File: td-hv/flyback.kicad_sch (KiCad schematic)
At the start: 54 parts, among them Q12 G3R450MT17J, U13 MCP1416

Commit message: td-hv 2.0 changes
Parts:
- removed TP11, TP5: TestPoint, TestPoint:TestPoint_Keystone_5019_Minature, symbol Connector:TestPoint
- added U? (x2): 74HC00, Package_SO:SOIC-14_3.9x8.7mm_P1.27mm, symbol 74xx:74HC00
- C?: footprint Capacitor_SMD:C_1206_3216Metric -> Capacitor_SMD:C_1812_4532Metric
- D?: footprint Diode_SMD:D_SMA -> Diode_THT:D_DO-41_SOD81_P10.16mm_Horizontal
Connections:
- net GND: now also U?.1, U?.1, U?.2, U?.2
- net eht out: now also R?.1; no longer C?.1
- net at C?.2, L?.2, Q?.1 (S)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: now also C?.2; no longer R?.2
- new net snub: C?.1, R?.2
- no-connect marks 4 -> 6
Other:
- moved on the sheet: C?, R?

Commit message: small bom changes
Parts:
- C?: Digikey 1276-3272-1-ND‎ -> 478-3005-1-ND
- D?: value ES1G-13-F -> DNP; footprint Diode_THT:D_DO-41_SOD81_P10.16mm_Horizontal -> Diode_SMD:D_SMA; symbol Diode:BA157 -> Diode:MRA4004T3G
- L?: Digikey (none) -> DNP
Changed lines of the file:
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@@
       (effects (font (size 1.27 1.27)) hide)
     )
-    (property "Digikey" "" (at 161.29 66.04 0)
+    (property "Digikey" "DNP" (at 161.29 66.04 0)
       (effects (font (size 1.27 1.27)) hide)
     )
@@
     )
   )
-  (symbol (lib_id "Diode:BA157") (at 109.22 44.45 180) (unit 1)
+  (symbol (lib_id "Diode:MRA4004T3G") (at 109.22 44.45 180) (unit 1)
     (in_bom yes) (on_board yes) (dnp no)
     (property "Reference" "D?" (at 109.22 38.9636 0)
       (effects (font (size 1.27 1.27)))
     )
-    (property "Value" "ES1G-13-F" (at 109.22 41.275 0)
-      (effects (font (size 1.27 1.27)))
-    )
-    (property "Footprint" "Diode_THT:D_DO-41_SOD81_P10.16mm_Horizontal" (at 109.22 40.005 0)
-      (effects (font (size 1.27 1.27)) hide)
-    )
-    (property "Datasheet" "https://www.vishay.com/docs/88536/ba157.pdf" (at 109.22 44.45 0)
+    (property "Value" "DNP" (at 109.22 41.275 0)
+      (effects (font (size 1.27 1.27)))
+    )
+    (property "Footprint" "Diode_SMD:D_SMA" (at 109.22 40.005 0)
+      (effects (font (size 1.27 1.27)) hide)
+    )
+    (property "Datasheet" "http://www.onsemi.com/pub_link/Collateral/MRA4003T3-D.PDF" (at 109.22 44.45 0)
       (effects (font (size 1.27 1.27)) hide)
     )
@@
       (effects (font (size 1.27 1.27)) hide)
     )
-    (property "Digikey" "1276-3272-1-ND‎" (at 144.78 54.61 0)
-      (effects (font (size 1.27 1.27)) hide)
-    )
+    (property "Digikey" "478-3005-1-ND" (at 144.78 54.61 0)
+      (effects (font (size 1.27 1.27)) hide)
+    )

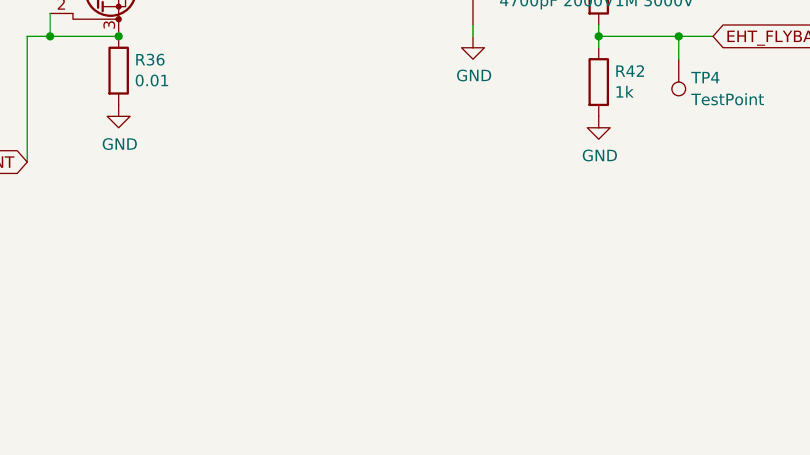
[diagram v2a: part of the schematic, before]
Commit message: add td-hv todo
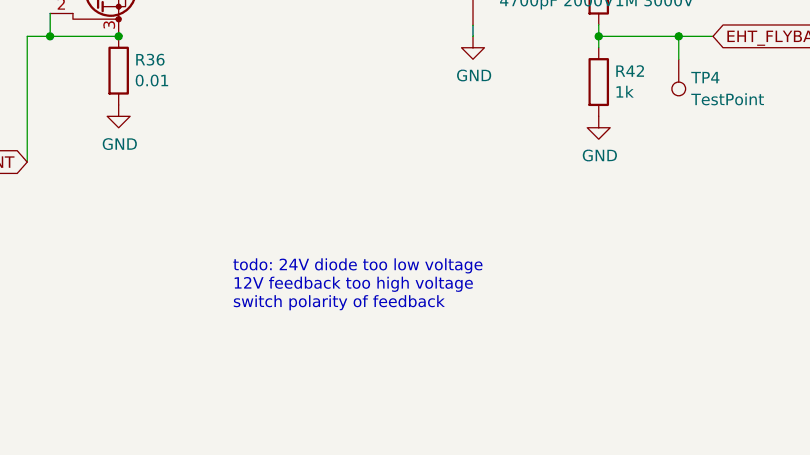
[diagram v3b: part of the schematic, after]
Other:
- note added: "todo: 24V diode too low voltage 12V feedback too high voltage switch polarity of feedback"
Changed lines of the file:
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@@
+    (effects (font (size 1.27 1.27)) (justify left bottom))
+  )
+  (text "todo: 24V diode too low voltage\n12V feedback too high voltage\nswitch polarity of feedback"
+    (at 162.56 148.59 0)
     (effects (font (size 1.27 1.27)) (justify left bottom))
   )

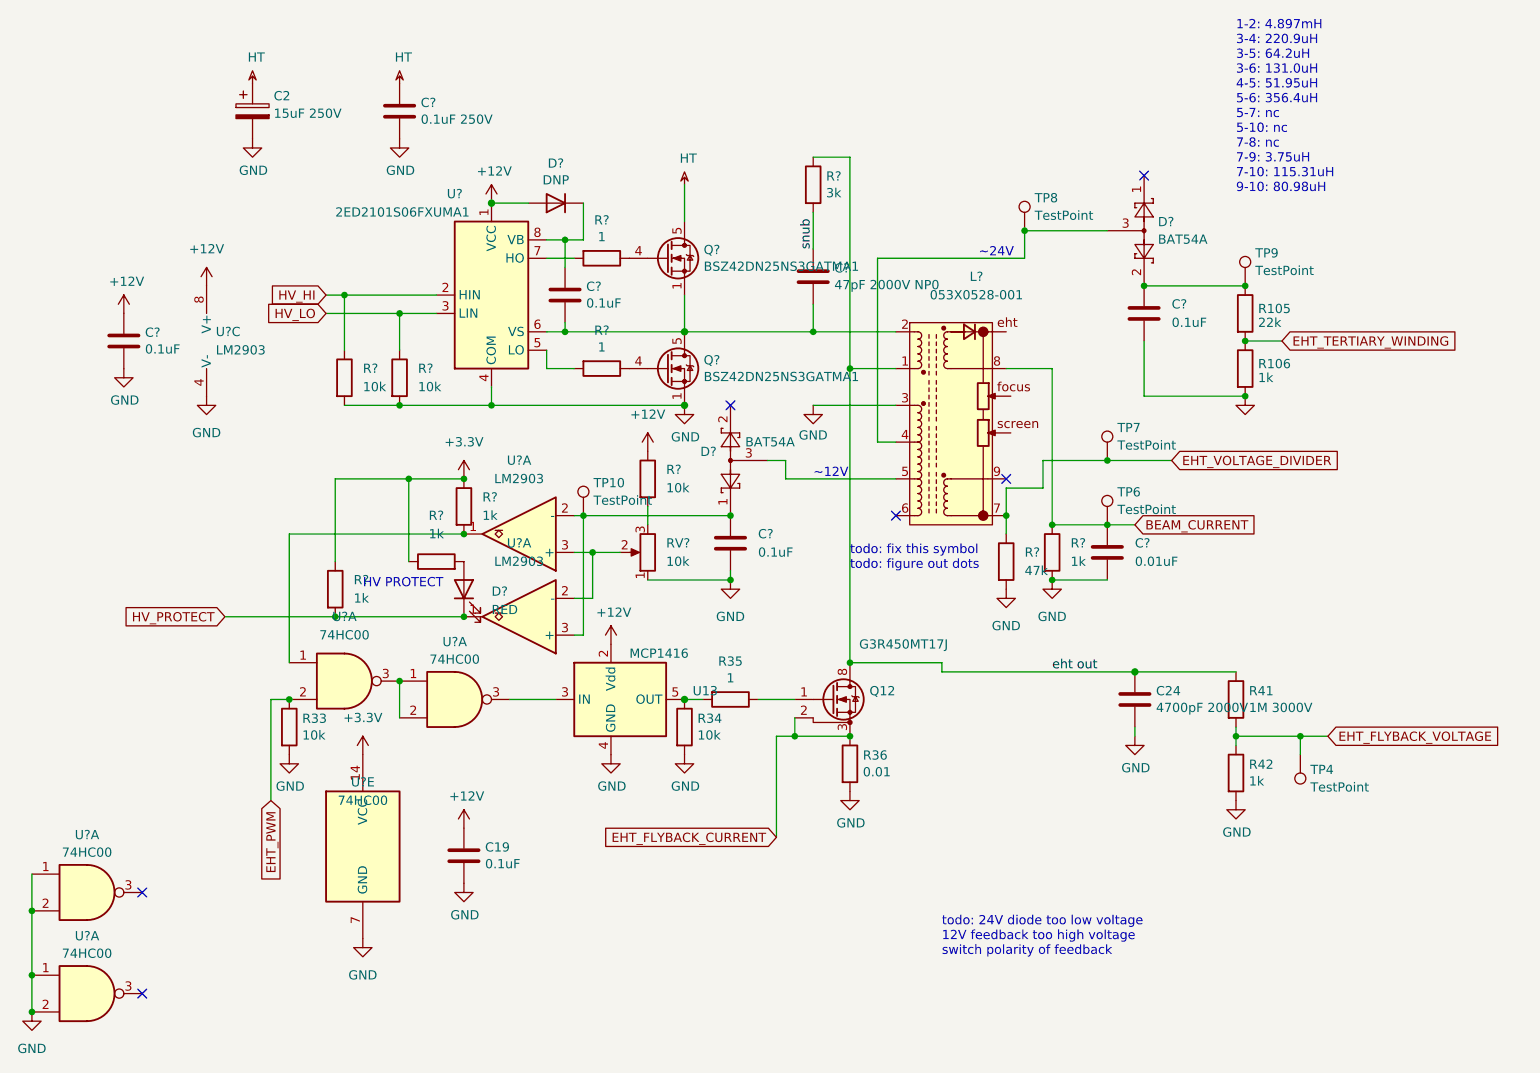
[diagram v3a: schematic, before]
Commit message: update td-hv to new format
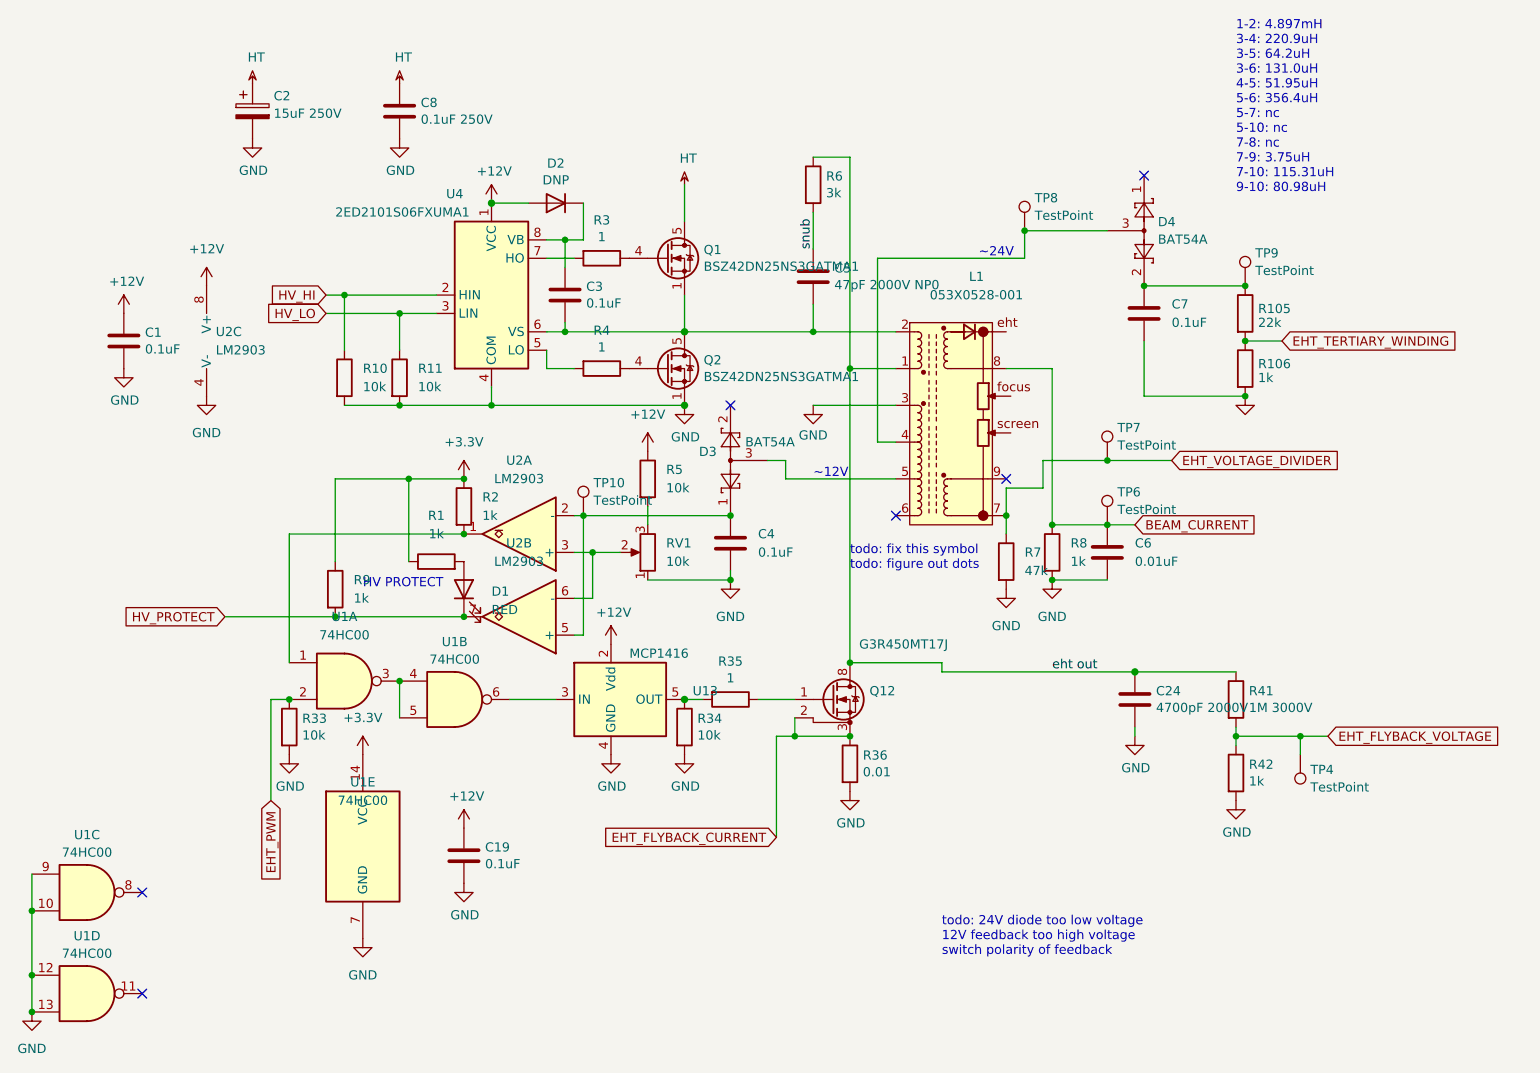
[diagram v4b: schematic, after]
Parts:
- gave numbers to parts that had none: 29
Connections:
- net GND: now also U1.10, U1.12, U1.13, U1.9; no longer U1.1, U1.1, U1.2, U1.2
- net HV_PROTECT: now also U2.7; no longer U2.1
- net at RV1.2, U2.3 (+): now also U2.6 (-); no longer U2.2 (-)
- net at C4.1, D3.1, TP10.1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: now also U2.5 (+); no longer U2.3 (+)
- net at U13.3 (IN): now also U1.6; no longer U1.3
- new net: U1.3, U1.4, U1.5

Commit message: do some basic fixes
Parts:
- TP10, TP4, TP6, TP7, TP8, TP9: footprint TestPoint:TestPoint_Keystone_5019_Minature -> TestPoint:TestPoint_Keystone_5019_Miniature
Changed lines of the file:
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@@
 			)
 		)
-		(property "Footprint" "TestPoint:TestPoint_Keystone_5019_Minature"
+		(property "Footprint" "TestPoint:TestPoint_Keystone_5019_Miniature"
 			(at 179.07 48.26 0)
 			(effects
@@
 			)
 		)
-		(property "Footprint" "TestPoint:TestPoint_Keystone_5019_Minature"
+		(property "Footprint" "TestPoint:TestPoint_Keystone_5019_Miniature"
 			(at 118.11 87.63 0)
 			(effects
@@
 			)
 		)
-		(property "Footprint" "TestPoint:TestPoint_Keystone_5019_Minature"
+		(property "Footprint" "TestPoint:TestPoint_Keystone_5019_Miniature"
 			(at 190.5 80.01 0)
 			(effects
@@
 			)
 		)
-		(property "Footprint" "TestPoint:TestPoint_Keystone_5019_Minature"
+		(property "Footprint" "TestPoint:TestPoint_Keystone_5019_Miniature"
 			(at 190.5 88.9 0)
 			(effects
@@
 			)
 		)
-		(property "Footprint" "TestPoint:TestPoint_Keystone_5019_Minature"
+		(property "Footprint" "TestPoint:TestPoint_Keystone_5019_Miniature"
 			(at 207.01 120.65 0)
 			(effects
@@
 			)
 		)
-		(property "Footprint" "TestPoint:TestPoint_Keystone_5019_Minature"
+		(property "Footprint" "TestPoint:TestPoint_Keystone_5019_Miniature"
 			(at 209.55 55.88 0)
 			(effects

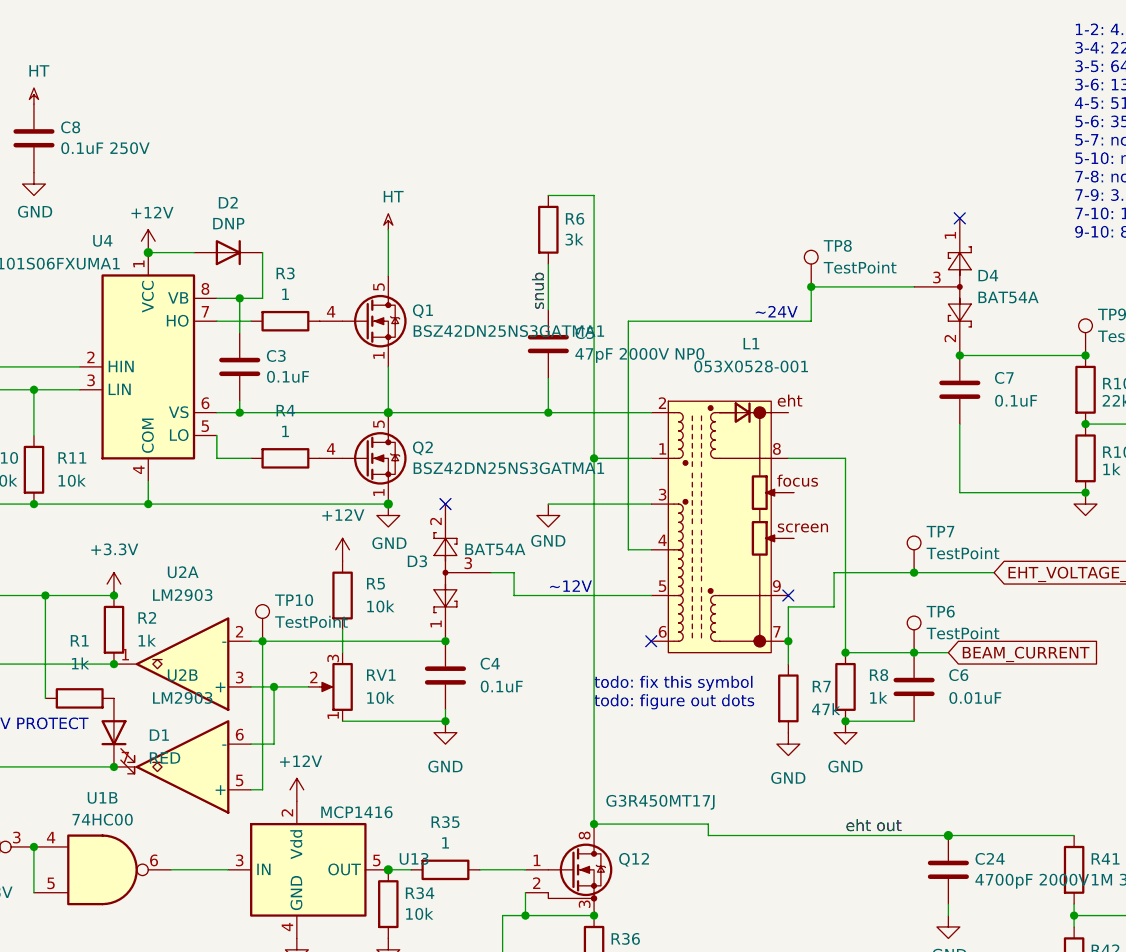
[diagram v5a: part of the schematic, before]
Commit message: Adjust td-hv pin spacing and add a bypass jumper
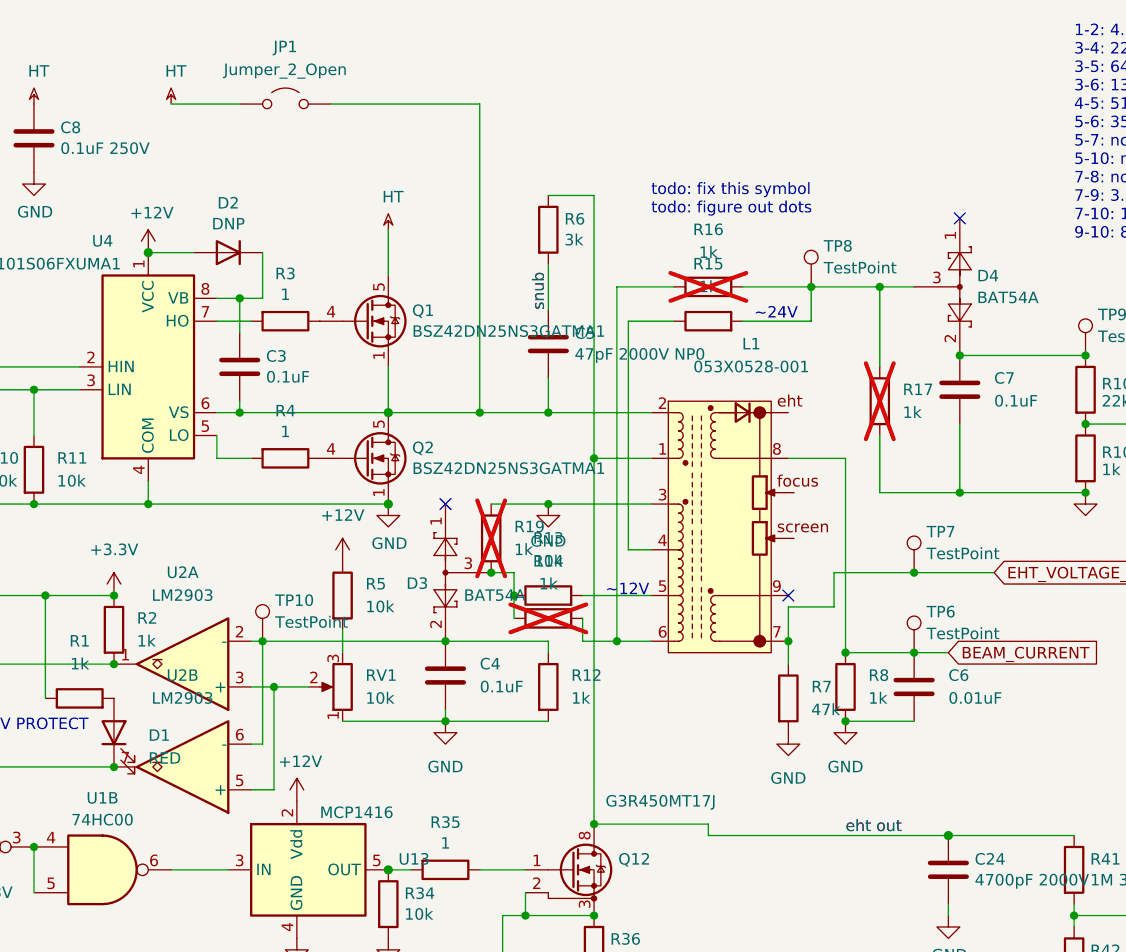
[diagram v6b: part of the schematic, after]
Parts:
- added JP1: Jumper_2_Open, Connector_PinHeader_2.54mm:PinHeader_1x02_P2.54mm_Vertical, symbol Jumper:Jumper_2_Open
- added R12, R14, R15, R16, R17, R19: 1k, Resistor_SMD:R_0805_2012Metric, symbol Device:R
- added R13: 10k, Resistor_SMD:R_0805_2012Metric, symbol Device:R
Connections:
- net GND: now also R12.2, R17.1, R19.2
- net HT: now also JP1.1 (A)
- net at RV1.2, U2.3 (+): now also U2.5 (+); no longer U2.6 (-)
- net at C3.2, C5.2, L1.2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: now also JP1.2 (B)
- net at C4.1, TP10.1, U2.2 (-): now also D3.2, U2.6 (-), R12.1; no longer D3.1, U2.5 (+)
- net at D3.3: now also R13.1, R14.1, R19.1; no longer L1.5
- net at D4.3, TP8.1: now also R15.2, R16.2, R17.2; no longer L1.4
- net at L1.6: now also R14.2, R16.1
- new net: L1.4, R15.1
- new net: L1.5, R13.2
- no-connect marks 6 -> 5

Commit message: update td-hv bom
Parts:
- C5: Digikey 478-3005-1-ND -> 478-4734-1-ND
- JP1: Digikey (none) -> DNP
- R12, R14, R15, R16, R17, R19: Digikey (none) -> 311-1.00KCRCT-ND
- R13: Digikey (none) -> 311-10.0KCRCT-ND
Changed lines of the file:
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@@
 			)
 		)
-		(property "Digikey" ""
+		(property "Digikey" " 311-1.00KCRCT-ND"
 			(at 162.56 52.07 0)
 			(effects
@@
 			)
 		)
-		(property "Digikey" ""
+		(property "Digikey" " 311-1.00KCRCT-ND"
 			(at 144.78 85.09 0)
 			(effects
@@
 			)
 		)
-		(property "Digikey" ""
+		(property "Digikey" " 311-1.00KCRCT-ND"
 			(at 162.56 48.26 0)
 			(effects
@@
 			)
 		)
-		(property "Digikey" ""
+		(property "Digikey" " 311-1.00KCRCT-ND"
 			(at 138.43 76.2 0)
 			(effects
@@
 			)
 		)
-		(property "Digikey" ""
+		(property "Digikey" " 311-1.00KCRCT-ND"
 			(at 144.78 92.71 0)
 			(effects
@@
 			)
 		)
-		(property "Digikey" ""
+		(property "Digikey" " 311-10.0KCRCT-ND"
 			(at 144.78 82.55 0)
 			(effects
@@
 			)
 		)
-		(property "Digikey" ""
+		(property "Digikey" " 311-1.00KCRCT-ND"
 			(at 181.61 60.96 0)
 			(effects
@@
 			)
 		)
+		(property "Digikey" "DNP"
+			(at 115.57 27.94 0)
+			(effects
+				(font
+					(size 1.27 1.27)
+				)
+				(hide yes)
+			)
+		)
 		(pin "1"
 		)
@@
 			)
 		)
-		(property "Digikey" "478-3005-1-ND"
+		(property "Digikey" "478-4734-1-ND"
 			(at 144.78 54.61 0)
 			(effects

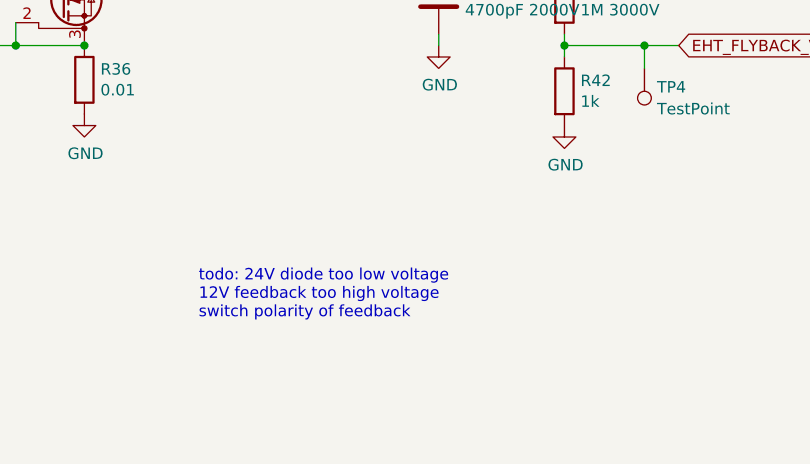
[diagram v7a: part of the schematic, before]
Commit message: adjust for nec monitor slightly
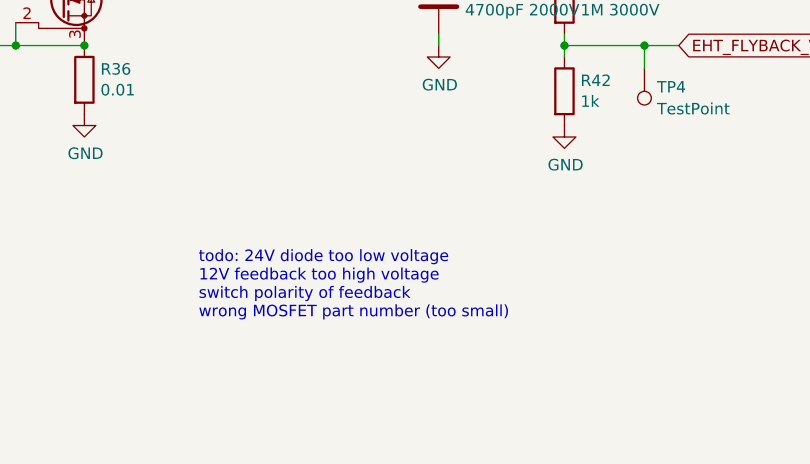
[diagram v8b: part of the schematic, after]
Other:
- note added: "todo: 24V diode too low voltage 12V feedback too high voltage switch polarity of feedback wrong MOSFET part number (too small)"
- note removed: "todo: 24V diode too low voltage 12V feedback too high voltage switch polarity of feedback"
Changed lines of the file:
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@@
 		)
 	)
-	(text "todo: 24V diode too low voltage\n12V feedback too high voltage\nswitch polarity of feedback"
+	(text "todo: 24V diode too low voltage\n12V feedback too high voltage\nswitch polarity of feedback\nwrong MOSFET part number (too small)"
 		(exclude_from_sim no)
 		(at 162.56 148.59 0)
